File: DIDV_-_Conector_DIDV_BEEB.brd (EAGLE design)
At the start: 80 x 34 mm, 6 parts

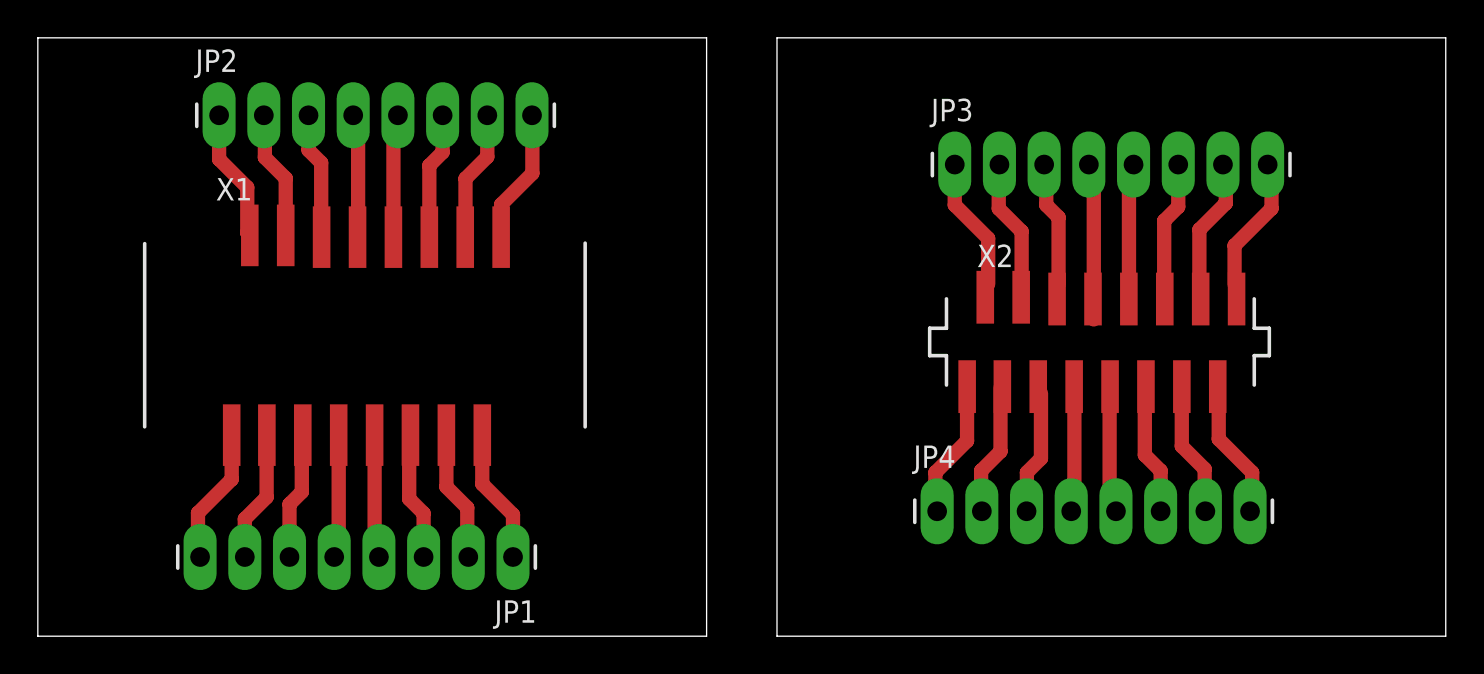
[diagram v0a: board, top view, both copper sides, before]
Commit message: Revisão 10
Revisão representa o estado final do projeto, alterações agora somente referentes a valores de componentes e adaptações se e somente se não existir a possibilidade de manobras via software.

Placas nas dimensões e condições as quais foram submetidas a cotação para confecção em local especializado.
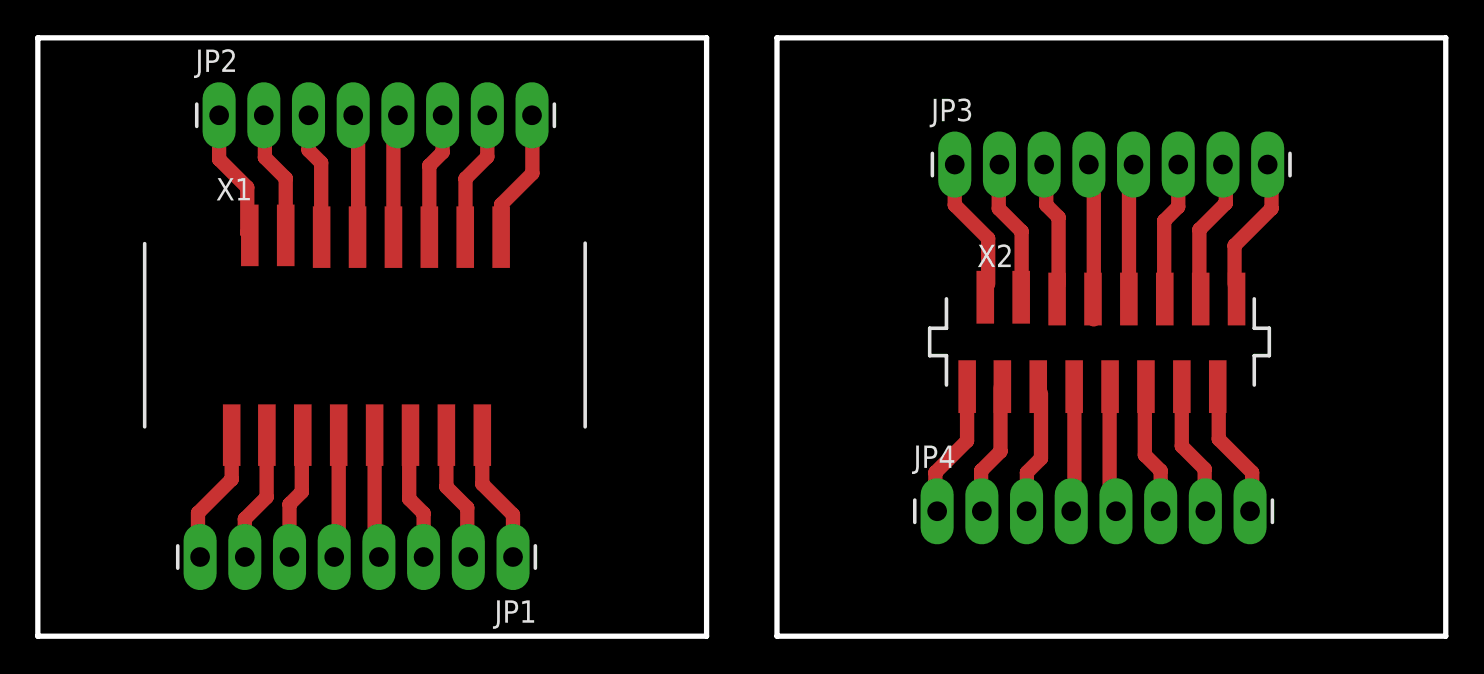
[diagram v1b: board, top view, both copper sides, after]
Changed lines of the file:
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@@
 <board>
 <plain>
-<wire x1="0" y1="0" x2="38" y2="0" width="0" layer="20"/>
-<wire x1="38" y1="0" x2="38" y2="34" width="0" layer="20"/>
-<wire x1="38" y1="34" x2="0" y2="34" width="0" layer="20"/>
-<wire x1="0" y1="34" x2="0" y2="0" width="0" layer="20"/>
-<wire x1="42" y1="0" x2="80" y2="0" width="0" layer="20"/>
-<wire x1="80" y1="0" x2="80" y2="34" width="0" layer="20"/>
-<wire x1="80" y1="34" x2="42" y2="34" width="0" layer="20"/>
-<wire x1="42" y1="34" x2="42" y2="0" width="0" layer="20"/>
+<wire x1="0" y1="0" x2="38" y2="0" width="0.3" layer="20"/>
+<wire x1="38" y1="0" x2="38" y2="34" width="0.3" layer="20"/>
+<wire x1="38" y1="34" x2="0" y2="34" width="0.3" layer="20"/>
+<wire x1="0" y1="34" x2="0" y2="0" width="0.3" layer="20"/>
+<wire x1="42" y1="0" x2="80" y2="0" width="0.3" layer="20"/>
+<wire x1="80" y1="0" x2="80" y2="34" width="0.3" layer="20"/>
+<wire x1="80" y1="34" x2="42" y2="34" width="0.3" layer="20"/>
+<wire x1="42" y1="34" x2="42" y2="0" width="0.3" layer="20"/>
 </plain>
 <attributes>
